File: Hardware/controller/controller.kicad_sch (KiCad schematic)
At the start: 26 parts, among them J101 Conn_02x10_Odd_Even, J102 Conn_02x10_Odd_Even, J103 Conn_02x10_Odd_Even, U101 PCA9543A

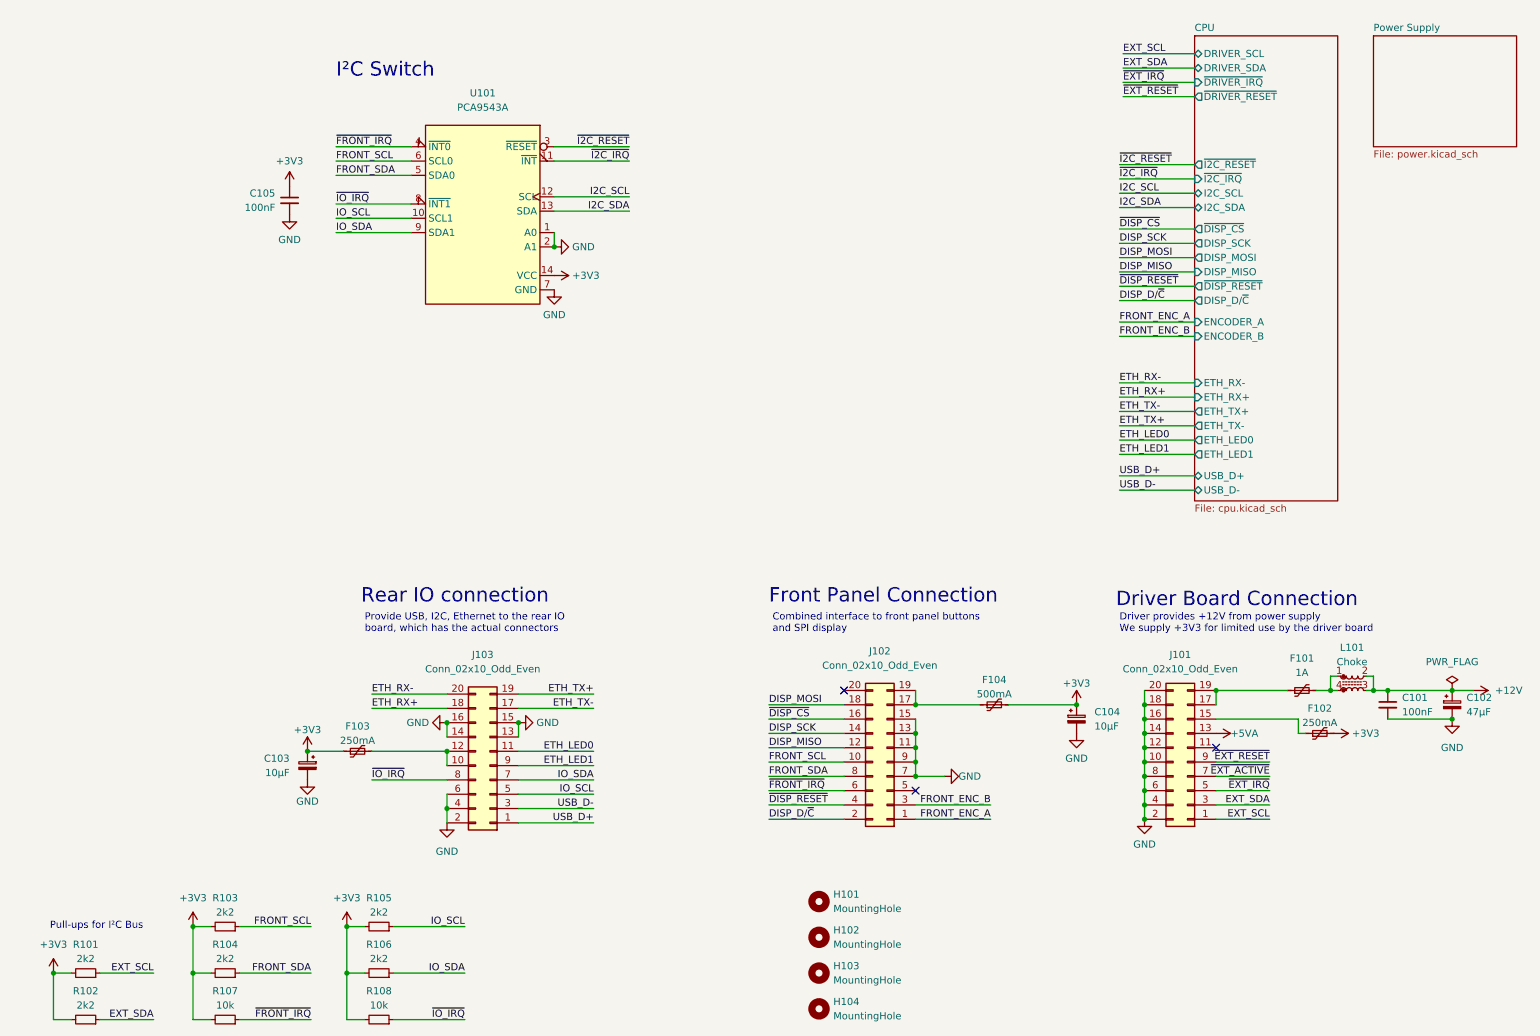
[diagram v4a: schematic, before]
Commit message: Added beeper to control board
- Added a beeper (magnetic transducer, including an amplifier to go with
  it) to the controller board so we can make loud annoying beeping
  noises as desired

- A few minor tweaks to the layout of the control board
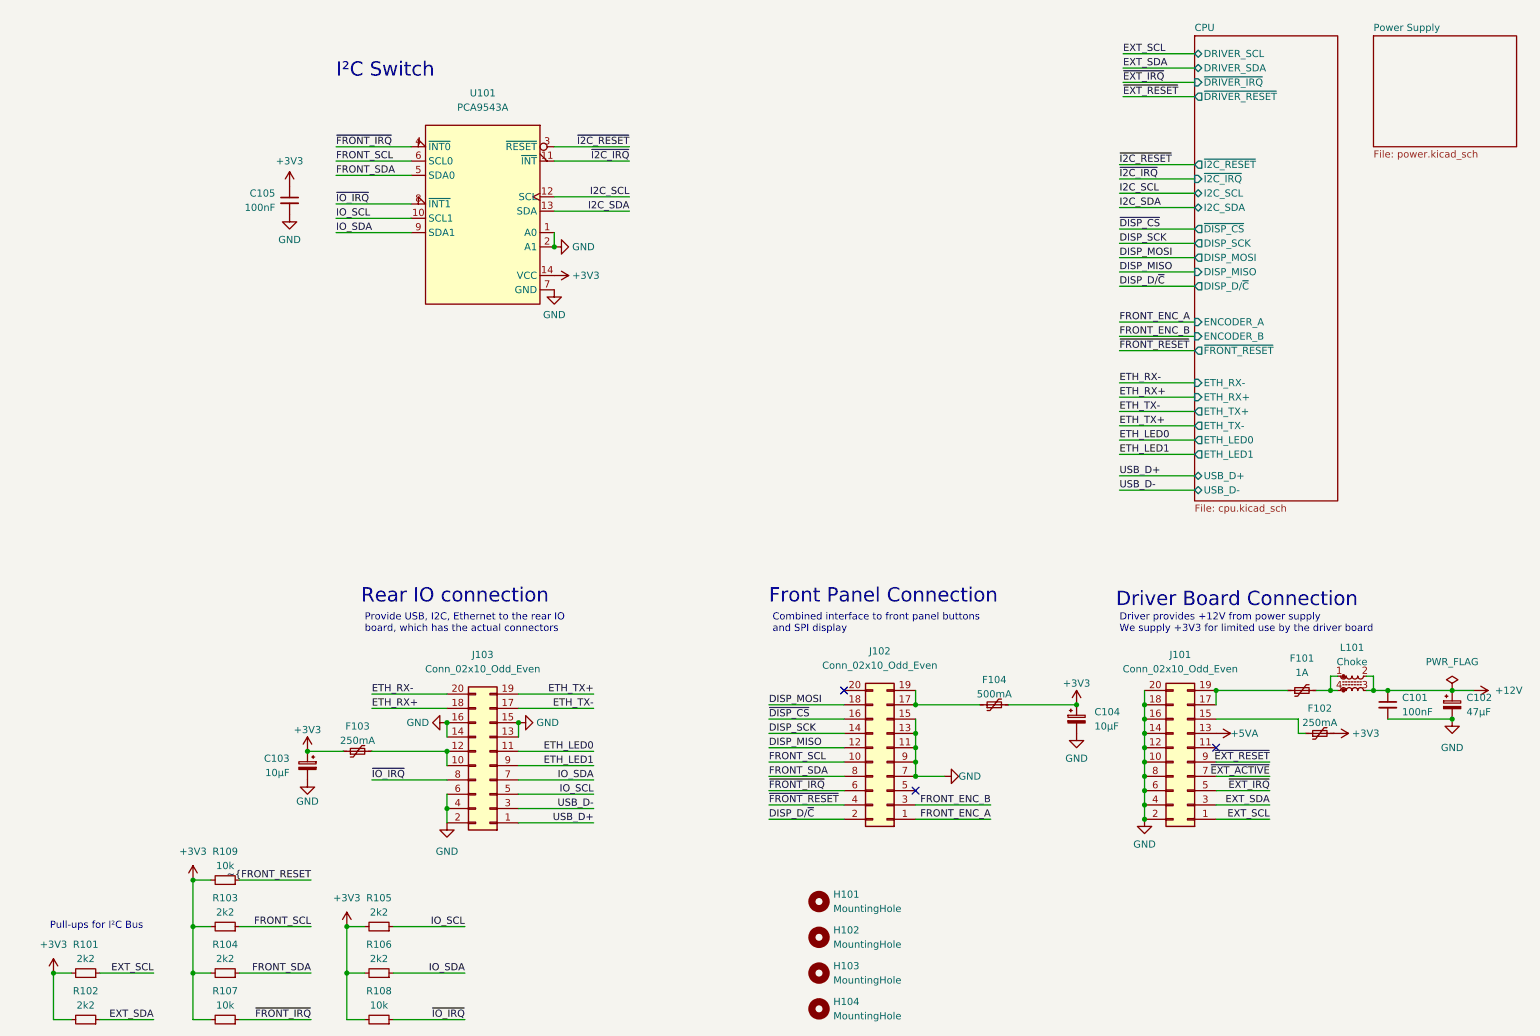
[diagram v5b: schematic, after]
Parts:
- added R109: 10k, Resistor_SMD:R_0805_2012Metric_Pad1.20x1.40mm_HandSolder, symbol Device:R_Small
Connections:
- net +3V3: now also R109.2
- net ~{DISP_RESET} renamed ~{FRONT_RESET}
- new net ~{FRONT_RESET: R109.1
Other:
- sheet CPU ports: added ~{FRONT_RESET}; removed ~{DISP_RESET}

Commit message: External trigger input
- Added a basic Schmitt-trigger based external trigger input. There's a
  basic pulse shaping circuit attached to it, before its fed into the
  buffer, and then off to the main board to use as an interrupt line to
  control the system mode.
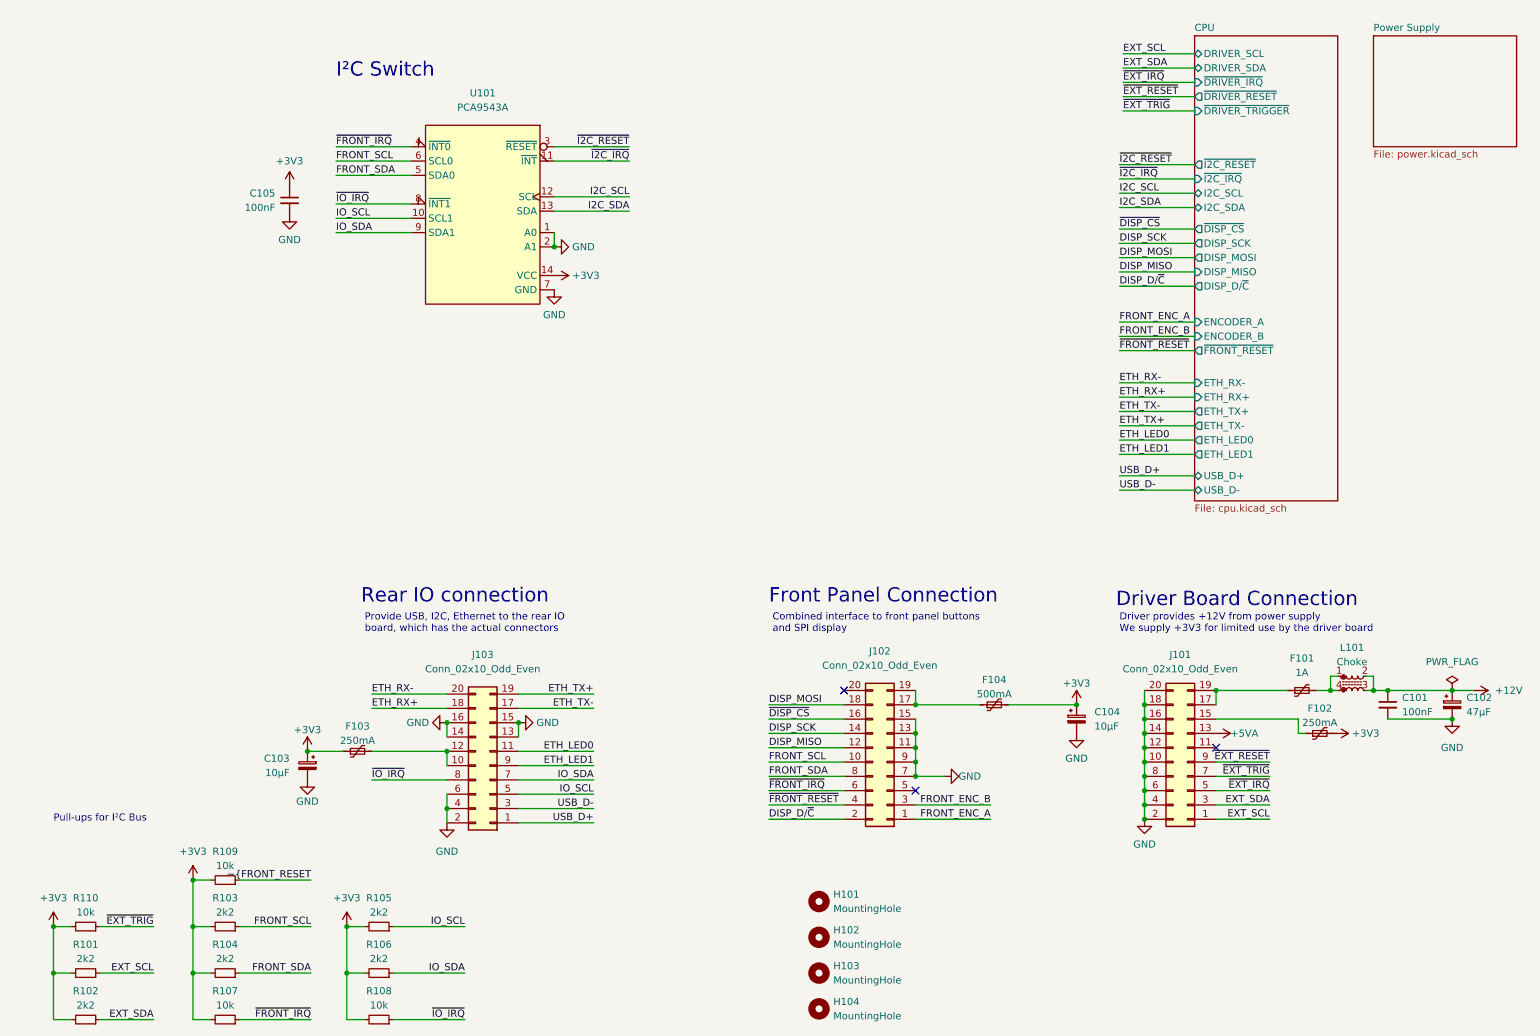
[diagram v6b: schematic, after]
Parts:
- added R110: 10k, Resistor_SMD:R_0805_2012Metric_Pad1.20x1.40mm_HandSolder, symbol Device:R_Small
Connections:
- net +3V3: now also R110.2
- net ~{EXT_ACTIVE} renamed ~{EXT_TRIG}
- net ~{EXT_TRIG}: now also R110.1
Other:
- sheet CPU ports: added ~{DRIVER_TRIGGER}; removed none
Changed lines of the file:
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@@
   (junction (at 213.36 140.335) (diameter 0) (color 0 0 0 0)
   )
+  (junction (at 19.685 185.42) (diameter 0) (color 0 0 0 0)
+  )
   (junction (at 64.77 146.05) (diameter 0) (color 0 0 0 0)
   )
@@
   (junction (at 108.585 56.515) (diameter 0) (color 0 0 0 0)
   )
-  (junction (at 19.685 185.42) (diameter 0) (color 0 0 0 0)
-  )
   (junction (at 213.36 150.495) (diameter 0) (color 0 0 0 0)
   )
@@
   )
   (junction (at 71.755 185.42) (diameter 0) (color 0 0 0 0)
+  )
+  (junction (at 19.685 177.165) (diameter 0) (color 0 0 0 0)
   )
   (junction (at 213.36 153.035) (diameter 0) (color 0 0 0 0)
@@
     (stroke (width 0) (type default) (color 0 0 0 0))
   )
+  (wire (pts (xy 222.25 32.385) (xy 209.55 32.385))
+    (stroke (width 0) (type default) (color 0 0 0 0))
+  )
   (wire (pts (xy 44.45 177.165) (xy 47.625 177.165))
     (stroke (width 0) (type default) (color 0 0 0 0))
@@
     (stroke (width 0) (type default) (color 0 0 0 0))
   )
+  (wire (pts (xy 19.685 177.165) (xy 19.685 185.42))
+    (stroke (width 0) (type default) (color 0 0 0 0))
+  )
   (wire (pts (xy 209.55 24.765) (xy 222.25 24.765))
     (stroke (width 0) (type default) (color 0 0 0 0))
@@
     (stroke (width 0) (type default) (color 0 0 0 0))
   )
+  (wire (pts (xy 22.86 177.165) (xy 19.685 177.165))
+    (stroke (width 0) (type default) (color 0 0 0 0))
+  )
   (wire (pts (xy 256.54 135.255) (xy 267.97 135.255))
     (stroke (width 0) (type default) (color 0 0 0 0))
@@
     (stroke (width 0) (type default) (color 0 0 0 0))
   )
+  (wire (pts (xy 37.465 177.165) (xy 27.94 177.165))
+    (stroke (width 0) (type default) (color 0 0 0 0))
+  )
   (wire (pts (xy 89.535 153.67) (xy 89.535 156.21))
     (stroke (width 0) (type default) (color 0 0 0 0))
@@
     (stroke (width 0) (type default) (color 0 0 0 0))
   )
-  (text "Pull-ups for I²C Bus\n" (at 19.05 177.8 0)
+  (text "Pull-ups for I²C Bus\n" (at 19.685 158.75 0)
     (effects (font (size 1.27 1.27)) (justify left bottom))
   )
@@
     (effects (font (size 1.27 1.27)) (justify left bottom))
   )
+  (label "~{EXT_TRIG}" (at 37.465 177.165 180)
+    (effects (font (size 1.27 1.27)) (justify right bottom))
+  )
   (label "ETH_RX+" (at 208.915 83.185 0)
     (effects (font (size 1.27 1.27)) (justify left bottom))
@@
     (effects (font (size 1.27 1.27)) (justify left bottom))
   )
-  (label "~{EXT_ACTIVE}" (at 235.585 150.495 180)
+  (label "~{EXT_TRIG}" (at 235.585 150.495 180)
     (effects (font (size 1.27 1.27)) (justify right bottom))
   )
@@
   (label "~{I2C_RESET}" (at 121.92 38.735 180)
     (effects (font (size 1.27 1.27)) (justify right bottom))
+  )
+  (label "~{EXT_TRIG}" (at 209.55 32.385 0)
+    (effects (font (size 1.27 1.27)) (justify left bottom))
   )
   (label "~{FRONT_RESET}" (at 146.685 155.575 0)
@@
     )
     (pin "1")
+  )
+  (symbol (lib_id "Device:R_Small") (at 25.4 177.165 270) (mirror x) (unit 1)
+    (in_bom yes) (on_board yes)
+    (property "Reference" "R110" (id 0) (at 25.4 172.085 90))
+    (property "Value" "10k" (id 1) (at 25.4 174.625 90))
+    (property "Footprint" "Resistor_SMD:R_0805_2012Metric_Pad1.20x1.40mm_HandSolder" (id 2) (at 25.4 177.165 0)
+      (effects (font (size 1.27 1.27)) hide)
+    )
+    (property "Datasheet" "~" (id 3) (at 25.4 177.165 0)
+      (effects (font (size 1.27 1.27)) hide)
+    )
+    (property "MPN" "RMC1/10-103JTP" (id 4) (at 25.4 177.165 90)
+      (effects (font (size 1.27 1.27)) hide)
+    )
+    (pin "1")
+    (pin "2")
   )
   (symbol (lib_id "Connector_Generic:Conn_02x10_Odd_Even") (at 97.155 148.59 180) (unit 1)
@@
     (pin "1")
   )
-  (symbol (lib_id "power:+3V3") (at 19.685 185.42 0) (unit 1)
-    (in_bom yes) (on_board yes) (fields_autoplaced)
-    (property "Reference" "#PWR0105" (id 0) (at 19.685 189.23 0)
-      (effects (font (size 1.27 1.27)) hide)
-    )
-    (property "Value" "+3V3" (id 1) (at 19.685 180.34 0))
-    (property "Footprint" "" (id 2) (at 19.685 185.42 0)
-      (effects (font (size 1.27 1.27)) hide)
-    )
-    (property "Datasheet" "" (id 3) (at 19.685 185.42 0)
+  (symbol (lib_id "power:+3V3") (at 19.685 177.165 0) (unit 1)
+    (in_bom yes) (on_board yes) (fields_autoplaced)
+    (property "Reference" "#PWR0105" (id 0) (at 19.685 180.975 0)
+      (effects (font (size 1.27 1.27)) hide)
+    )
+    (property "Value" "+3V3" (id 1) (at 19.685 172.085 0))
+    (property "Footprint" "" (id 2) (at 19.685 177.165 0)
+      (effects (font (size 1.27 1.27)) hide)
+    )
+    (property "Datasheet" "" (id 3) (at 19.685 177.165 0)
       (effects (font (size 1.27 1.27)) hide)
     )
@@
       (effects (font (size 1.27 1.27)) (justify left))
     )
+    (pin "~{DRIVER_TRIGGER}" input (at 222.25 32.385 180)
+      (effects (font (size 1.27 1.27)) (justify left))
+    )
   )
   (sheet (at 254 19.05) (size 25.4 19.685) (fields_autoplaced)
@@
       (reference "R109") (unit 1) (value "10k") (footprint "Resistor_SMD:R_0805_2012Metric_Pad1.20x1.40mm_HandSolder")
     )
+    (path "/11da7628-8f29-42d4-862e-2ff4a3a6e6d2"
+      (reference "R110") (unit 1) (value "10k") (footprint "Resistor_SMD:R_0805_2012Metric_Pad1.20x1.40mm_HandSolder")
+    )
     (path "/b7fd8d9f-f2af-4339-978a-b429d8a8def6/92f6f638-55af-481a-b7ad-667d55b168c7"

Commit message: Controller board fan controller
- Added a fan controller (the same EMC2101-R as on the driver) to the
  controller board, to control the rear case fan. This is driven off the
  rear IO I2C bus, which itself is switched behind the "auxiliary" I2C
  bus.
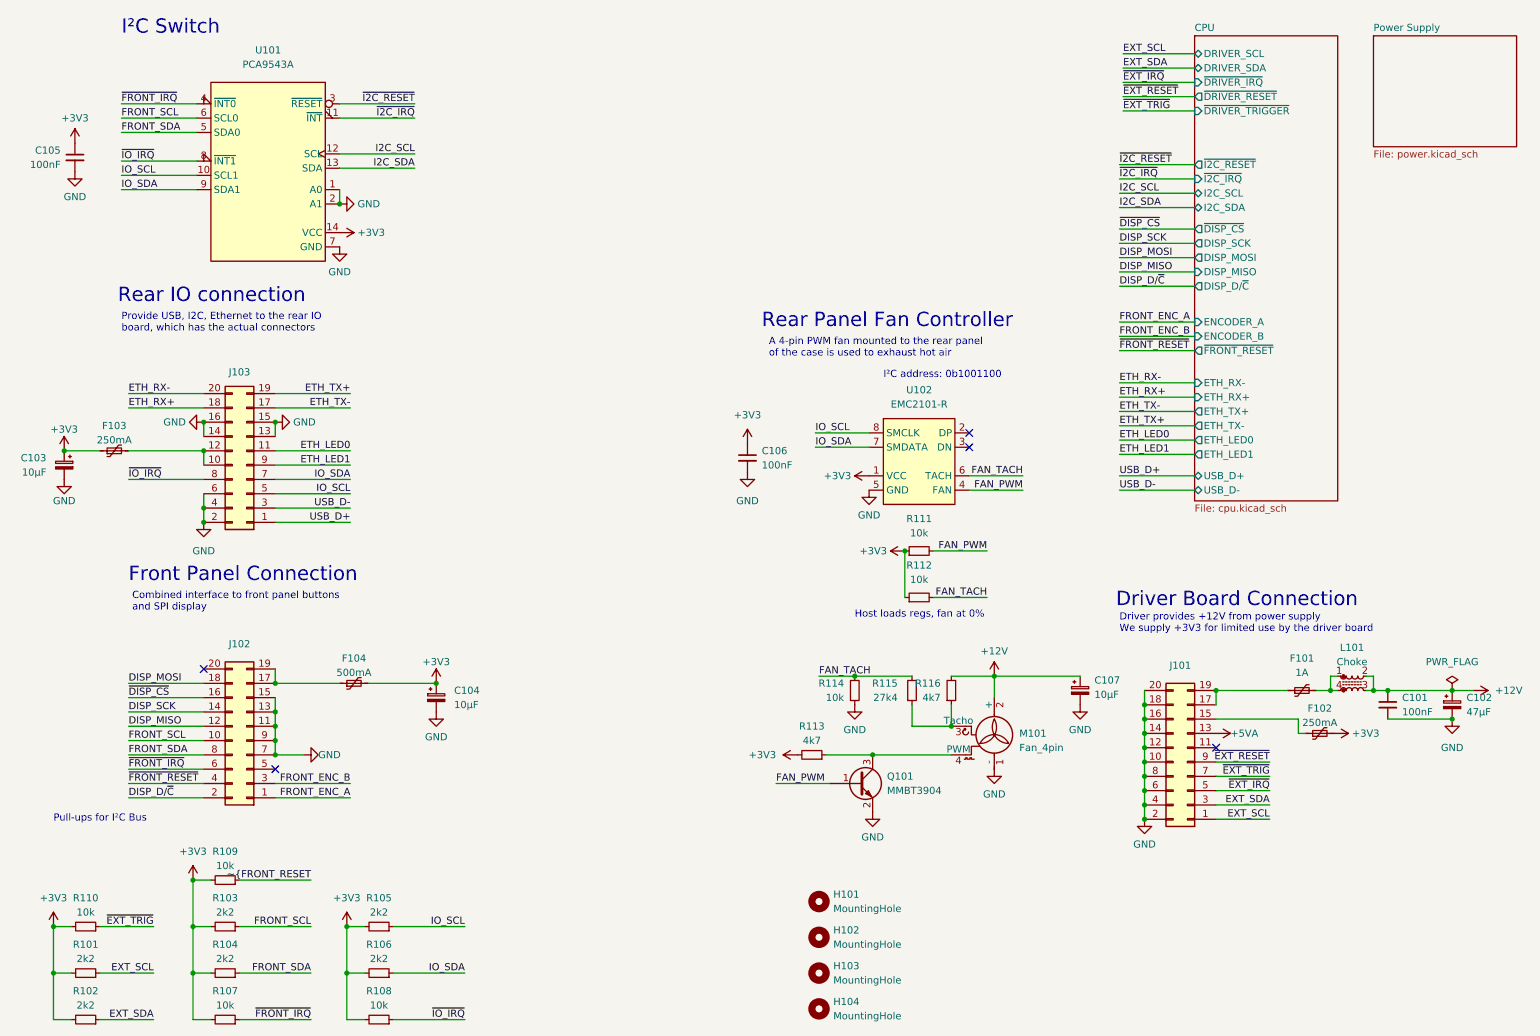
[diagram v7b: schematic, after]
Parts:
- added C106: 100nF, Capacitor_SMD:C_0805_2012Metric_Pad1.18x1.45mm_HandSolder, symbol Device:C_Small
- added C107: 10µF, Capacitor_THT:CP_Radial_D5.0mm_P2.00mm, symbol Device:C_Polarized_Small
- added M101: Fan_4pin, Connector_Molex:Molex_KK-254_AE-6410-04A_1x04_P2.54mm_Vertical, symbol Motor:Fan_4pin
- added Q101: MMBT3904, Package_TO_SOT_SMD:SOT-23, symbol Transistor_BJT:MMBT3904
- added R111, R112, R114: 10k, Resistor_SMD:R_0805_2012Metric_Pad1.20x1.40mm_HandSolder, symbol Device:R_Small
- added R113, R116: 4k7, Resistor_SMD:R_0805_2012Metric_Pad1.20x1.40mm_HandSolder, symbol Device:R_Small
- added R115: 27k4, Resistor_SMD:R_0805_2012Metric_Pad1.20x1.40mm_HandSolder, symbol Device:R_Small
- added U102: EMC2101-R, Package_SO:MSOP-8_3x3mm_P0.65mm, symbol programmable-load:EMC2101-R
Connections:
- net +12V: now also C107.1, M101.2 (+), R116.2
- net +3V3: now also C106.1, R111.1, R112.1, R113.2, U102.1 (VCC)
- net GND: now also C106.2, C107.2, M101.1 (-), Q101.2 (E), R114.1, U102.5 (GND)
- net IO_SCL: now also U102.8 (SMCLK)
- net IO_SDA: now also U102.7 (SMDATA)
- new net: M101.4 (PWM), Q101.3 (C), R113.1
- new net: M101.3 (Tacho), R115.1, R116.1
- new net FAN_PWM: Q101.1 (B), R111.2, U102.4 (FAN)
- new net FAN_TACH: R112.2, R114.2, R115.2, U102.6 (TACH)
- no-connect marks 3 -> 5
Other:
- note added: "A 4-pin PWM fan mounted to the rear panel of the case is used to exhaust hot air"
- note added: "Host loads regs, fan at 0%"
- note added: "I²C address: 0b1001100"
- note added: "Rear Panel Fan Controller"
- moved on the sheet: C103, C104, C105, F103, F104, J102, J103, U101
